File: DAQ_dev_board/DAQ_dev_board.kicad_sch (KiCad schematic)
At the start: 38 parts, among them J1 Thermocouple, J2 Conn_01x16_Pin, J3 Conn_01x08_Pin, J5 Conn_01x08_Pin, U1 ADS1158IRTCR (ADC), U2 AD8495 (TC AMP), U3 OP777ARZ (OP AMP), Y1 32.768kHz

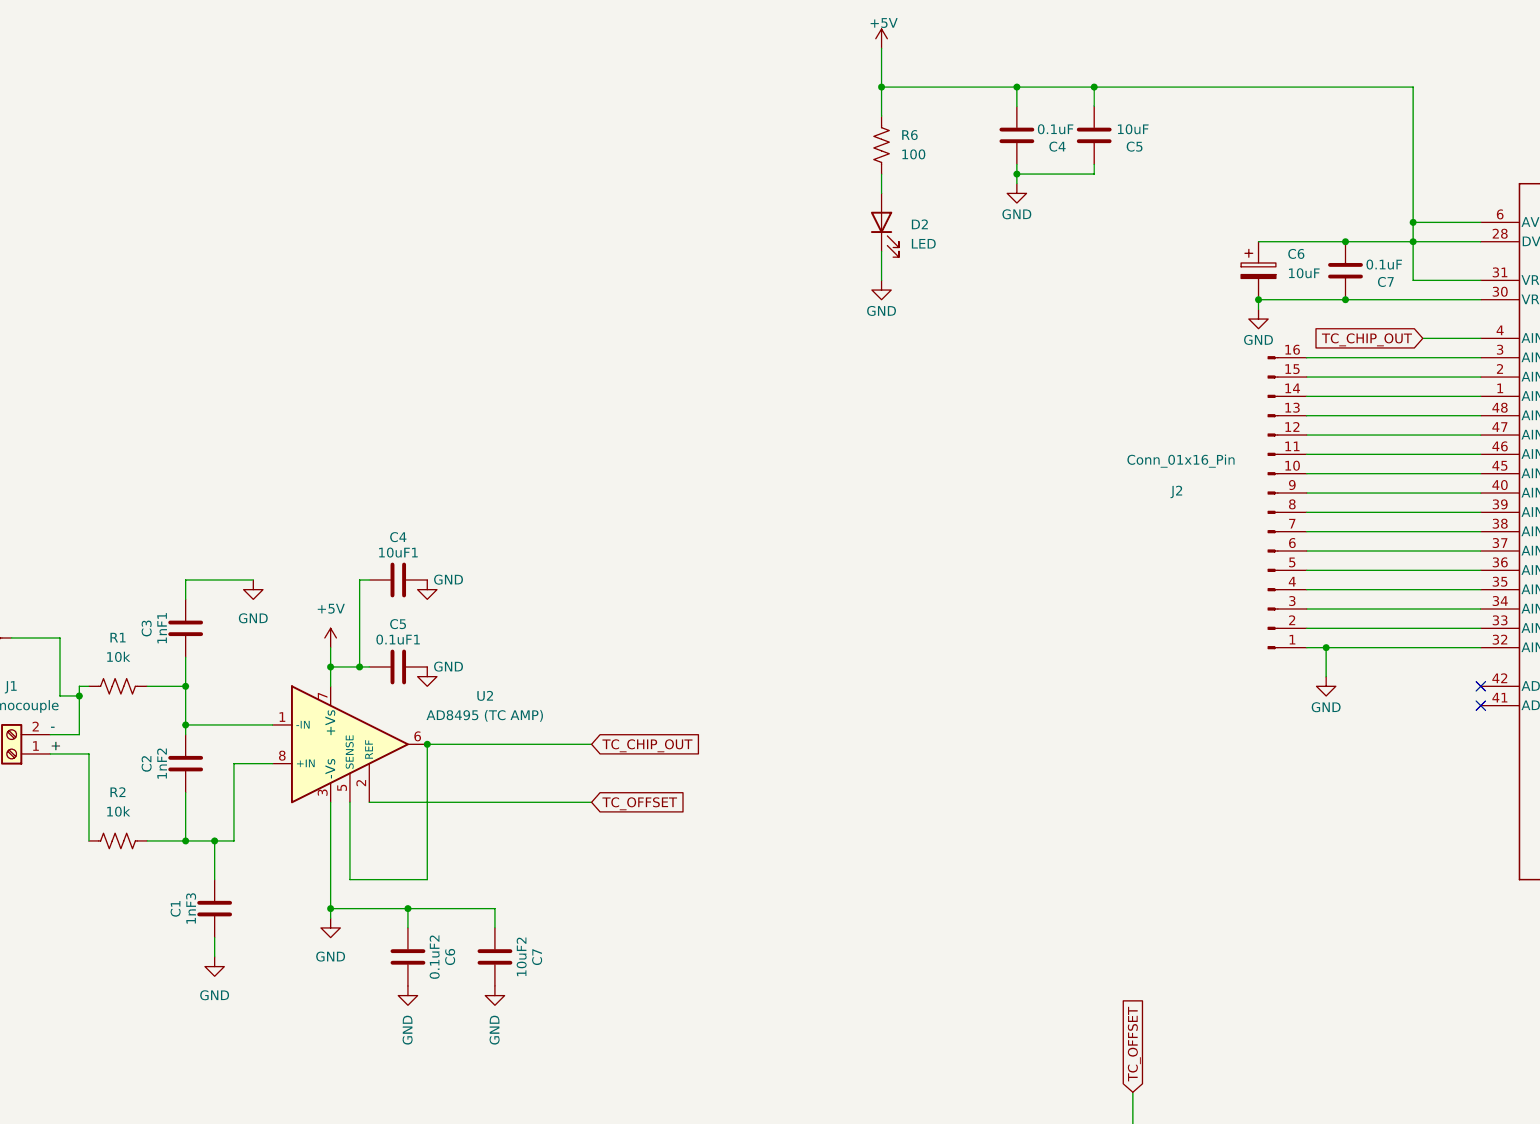
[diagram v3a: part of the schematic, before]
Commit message: updated DAQ silkscreen to be less dumb
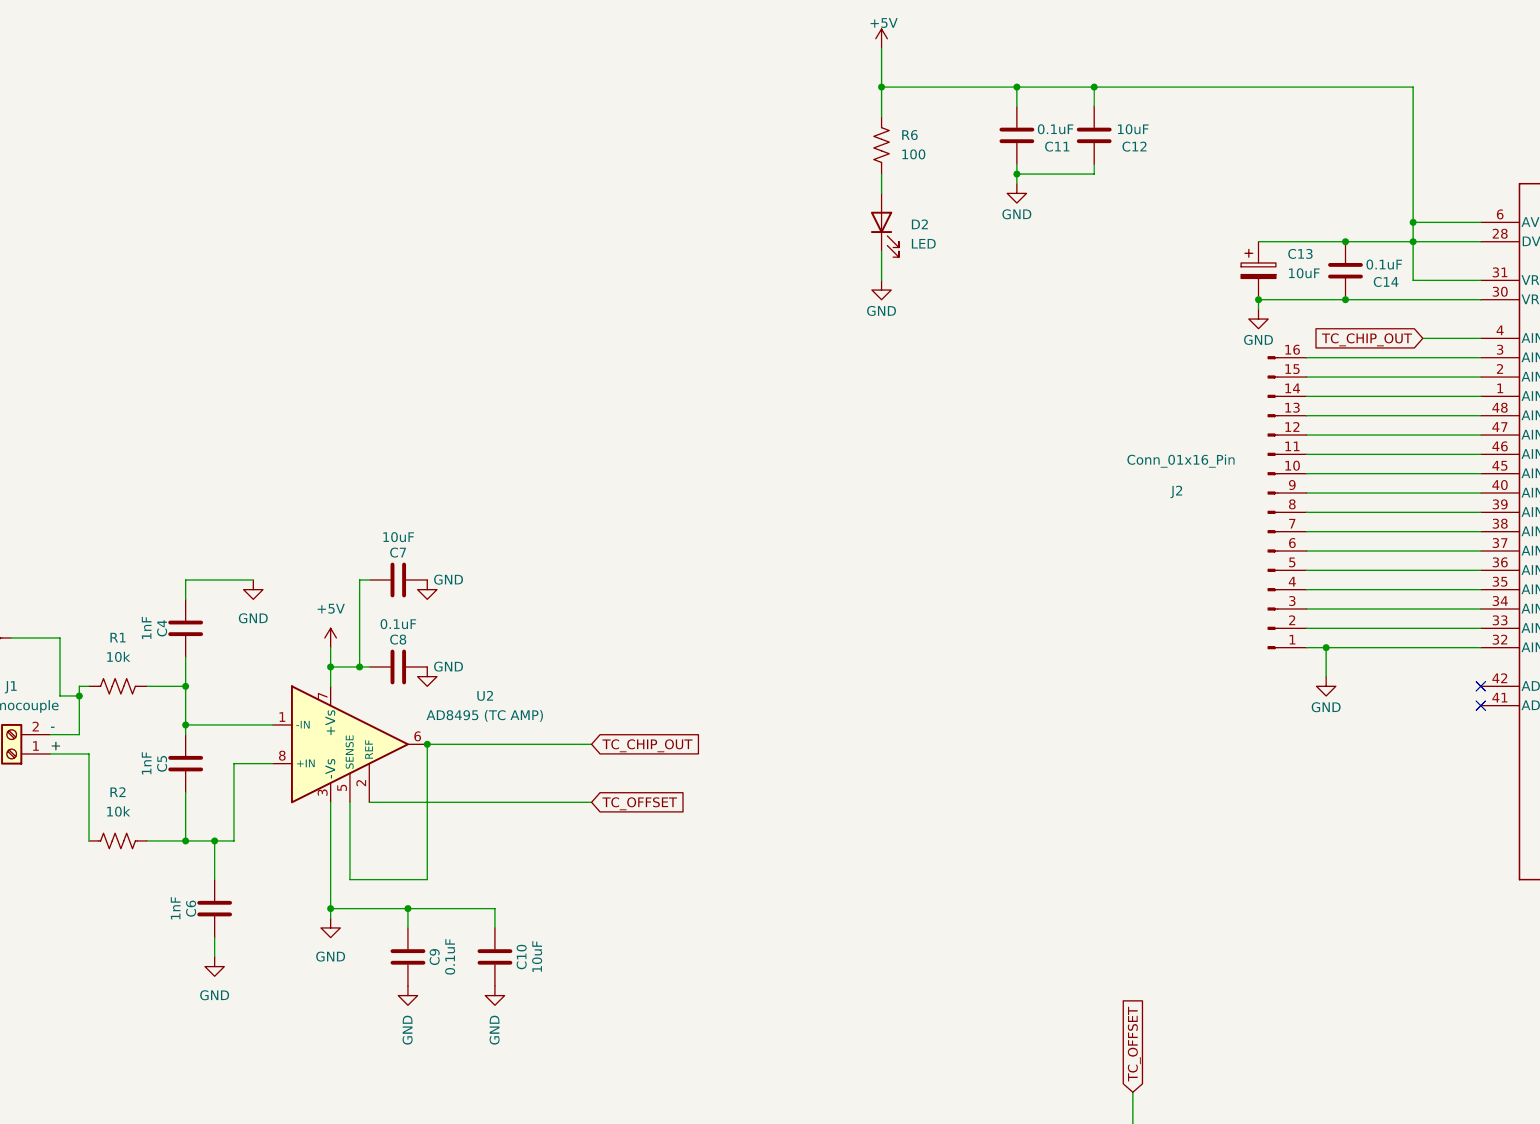
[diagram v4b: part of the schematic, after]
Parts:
- C10: renamed from 10uF2; value C7 -> 10uF
- C13: renamed from C6; footprint (none) -> Capacitor_SMD:C_0603_1608Metric
- C4: renamed from 1nF1; value C3 -> 1nF
- C5: renamed from 1nF2; value C2 -> 1nF
- C6: renamed from 1nF3; value C1 -> 1nF
- C7: renamed from 10uF1; value C4 -> 10uF
- C8: renamed from 0.1uF1; value C5 -> 0.1uF
- C9: renamed from 0.1uF2; value C6 -> 0.1uF
- R1, R10, R11, R12, R13, R14, R2, R3, R4, R5, R6, R7, R8, R9: footprint Capacitor_SMD:C_0603_1608Metric -> Resistor_SMD:R_0201_0603Metric
- renumbered C4 to C11, C5 to C12, C7 to C14
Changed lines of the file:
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@@
 			)
 		)
-		(property "Footprint" "Capacitor_SMD:C_0603_1608Metric"
+		(property "Footprint" "Resistor_SMD:R_0201_0603Metric"
 			(at 119.126 200.914 90)
 			(effects
@@
 		(on_board yes)
 		(dnp no)
-		(property "Reference" "10uF1"
+		(property "Reference" "C7"
 			(at 90.17 100.584 90)
 			(effects
@@
 			)
 		)
-		(property "Value" "C4"
+		(property "Value" "10uF"
 			(at 90.17 98.552 90)
 			(effects
@@
 			(project "DAQ_dev_board"
 				(path "/a39f2c3e-c1f4-493f-bbb6-b1b089f205f8"
-					(reference "10uF1")
+					(reference "C7")
 					(unit 1)
 				)
@@
 		(on_board yes)
 		(dnp no)
-		(property "Reference" "C4"
+		(property "Reference" "C11"
 			(at 176.784 47.244 0)
 			(effects
@@
 			(project "DAQ_dev_board"
 				(path "/a39f2c3e-c1f4-493f-bbb6-b1b089f205f8"
-					(reference "C4")
+					(reference "C11")
 					(unit 1)
 				)
@@
 			)
 		)
-		(property "Footprint" "Capacitor_SMD:C_0603_1608Metric"
+		(property "Footprint" "Resistor_SMD:R_0201_0603Metric"
 			(at 340.106 52.324 90)
 			(effects
@@
 			)
 		)
-		(property "Footprint" "Capacitor_SMD:C_0603_1608Metric"
+		(property "Footprint" "Resistor_SMD:R_0201_0603Metric"
 			(at 119.126 222.504 90)
 			(effects
@@
 			)
 		)
-		(property "Footprint" "Capacitor_SMD:C_0603_1608Metric"
+		(property "Footprint" "Resistor_SMD:R_0201_0603Metric"
 			(at 347.726 52.324 90)
 			(effects
@@
 			)
 		)
-		(property "Footprint" "Capacitor_SMD:C_0603_1608Metric"
+		(property "Footprint" "Resistor_SMD:R_0201_0603Metric"
 			(at 53.594 117.094 90)
 			(effects
@@
 			)
 		)
-		(property "Footprint" "Capacitor_SMD:C_0603_1608Metric"
+		(property "Footprint" "Resistor_SMD:R_0201_0603Metric"
 			(at 355.346 52.324 90)
 			(effects
@@
 			)
 		)
-		(property "Footprint" "Capacitor_SMD:C_0603_1608Metric"
+		(property "Footprint" "Resistor_SMD:R_0201_0603Metric"
 			(at 154.686 47.244 90)
 			(effects
@@
 		(on_board yes)
 		(dnp no)
-		(property "Reference" "1nF2"
+		(property "Reference" "C5"
 			(at 59.182 128.27 90)
 			(effects
@@
 			)
 		)
-		(property "Value" "C2"
+		(property "Value" "1nF"
 			(at 57.15 128.27 90)
 			(effects
@@
 			(project "DAQ_dev_board"
 				(path "/a39f2c3e-c1f4-493f-bbb6-b1b089f205f8"
-					(reference "1nF2")
+					(reference "C5")
 					(unit 1)
 				)
@@
 		(on_board yes)
 		(dnp no)
-		(property "Reference" "C5"
+		(property "Reference" "C12"
 			(at 186.944 47.244 0)
 			(effects
@@
 			(project "DAQ_dev_board"
 				(path "/a39f2c3e-c1f4-493f-bbb6-b1b089f205f8"
-					(reference "C5")
+					(reference "C12")
 					(unit 1)
 				)
@@
 			)
 		)
-		(property "Footprint" "Capacitor_SMD:C_0603_1608Metric"
+		(property "Footprint" "Resistor_SMD:R_0201_0603Metric"
 			(at 280.924 47.244 90)
 			(effects
@@
 			)
 		)
-		(property "Footprint" "Capacitor_SMD:C_0603_1608Metric"
+		(property "Footprint" "Resistor_SMD:R_0201_0603Metric"
 			(at 324.866 52.324 90)
 			(effects
@@
 		(on_board yes)
 		(dnp no)
-		(property "Reference" "C7"
+		(property "Reference" "C14"
 			(at 219.964 65.024 0)
 			(effects
@@
 			(project "DAQ_dev_board"
 				(path "/a39f2c3e-c1f4-493f-bbb6-b1b089f205f8"
-					(reference "C7")
+					(reference "C14")
 					(unit 1)
 				)
@@
 		(dnp no)
 		(fields_autoplaced yes)
-		(property "Reference" "C6"
+		(property "Reference" "C13"
 			(at 207.01 61.3409 0)
 			(effects
@@
 			)
 		)
-		(property "Footprint" ""
+		(property "Footprint" "Capacitor_SMD:C_0603_1608Metric"
 			(at 204.1652 67.31 0)
 			(effects
@@
 			(project ""
 				(path "/a39f2c3e-c1f4-493f-bbb6-b1b089f205f8"
-					(reference "C6")
+					(reference "C13")
 					(unit 1)
 				)
@@
 		(on_board yes)
 		(dnp no)
-		(property "Reference" "1nF1"
+		(property "Reference" "C4"
 			(at 59.182 110.49 90)
 			(effects
@@
 			)
 		)
-		(property "Value" "C3"
+		(property "Value" "1nF"
 			(at 57.15 110.49 90)
 			(effects
@@
 			(project ""
 				(path "/a39f2c3e-c1f4-493f-bbb6-b1b089f205f8"
-					(reference "1nF1")
+					(reference "C4")
 					(unit 1)
 				)
@@
 			)
 		)
-		(property "Footprint" "Capacitor_SMD:C_0603_1608Metric"
+		(property "Footprint" "Resistor_SMD:R_0201_0603Metric"
 			(at 35.814 110.744 90)
 			(effects
@@
 			)
 		)
-		(property "Footprint" "Capacitor_SMD:C_0603_1608Metric"
+		(property "Footprint" "Resistor_SMD:R_0201_0603Metric"
 			(at 309.626 52.324 90)
 			(effects
@@
 		(on_board yes)
 		(dnp no)
-		(property "Reference" "1nF3"
+		(property "Reference" "C6"
 			(at 62.992 147.32 90)
 			(effects
@@
 			)
 		)
-		(property "Value" "C1"
+		(property "Value" "1nF"
 			(at 60.96 147.32 90)
 			(effects
@@
 			(project "DAQ_dev_board"
 				(path "/a39f2c3e-c1f4-493f-bbb6-b1b089f205f8"
-					(reference "1nF3")
+					(reference "C6")
 					(unit 1)
 				)
@@
 		(on_board yes)
 		(dnp no)
-		(property "Reference" "0.1uF1"
+		(property "Reference" "C8"
 			(at 90.17 112.014 90)
 			(effects
@@
 			)
 		)
-		(property "Value" "C5"
+		(property "Value" "0.1uF"
 			(at 90.17 109.982 90)
 			(effects
@@
 			(project "DAQ_dev_board"
 				(path "/a39f2c3e-c1f4-493f-bbb6-b1b089f205f8"
-					(reference "0.1uF1")
+					(reference "C8")
 					(unit 1)
 				)
@@
 		(on_board yes)
 		(dnp no)
-		(property "Reference" "0.1uF2"
+		(property "Reference" "C9"
 			(at 94.996 153.67 90)
 			(effects
@@
 			)
 		)
-		(property "Value" "C6"
+		(property "Value" "0.1uF"
 			(at 97.028 153.67 90)
 			(effects
@@
 			(project "DAQ_dev_board"
 				(path "/a39f2c3e-c1f4-493f-bbb6-b1b089f205f8"
-					(reference "0.1uF2")
+					(reference "C9")
 					(unit 1)
 				)
@@
 		(on_board yes)
 		(dnp no)
-		(property "Reference" "10uF2"
+		(property "Reference" "C10"
 			(at 106.426 153.67 90)
 			(effects
@@
 			)
 		)
-		(property "Value" "C7"
+		(property "Value" "10uF"
 			(at 108.458 153.67 90)
 			(effects
@@
 			(project "DAQ_dev_board"
 				(path "/a39f2c3e-c1f4-493f-bbb6-b1b089f205f8"
-					(reference "10uF2")
+					(reference "C10")
 					(unit 1)
 				)
@@
 			)
 		)
-		(property "Footprint" "Capacitor_SMD:C_0603_1608Metric"
+		(property "Footprint" "Resistor_SMD:R_0201_0603Metric"
 			(at 332.486 52.324 90)
 			(effects
@@
 			)
 		)
-		(property "Footprint" "Capacitor_SMD:C_0603_1608Metric"
+		(property "Footprint" "Resistor_SMD:R_0201_0603Metric"
 			(at 53.594 137.414 90)
 			(effects
@@
 			)
 		)
-		(property "Footprint" "Capacitor_SMD:C_0603_1608Metric"
+		(property "Footprint" "Resistor_SMD:R_0201_0603Metric"
 			(at 317.246 52.324 90)
 			(effects
